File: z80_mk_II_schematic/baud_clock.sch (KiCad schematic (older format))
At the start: 9 parts

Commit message: Lots more work on schematic
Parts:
- gave numbers to parts that had none: 7
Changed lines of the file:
@@
 P 3350 3650
 AR Path="/5F996112/6026683D/602A193D" Ref="U?"  Part="1"
-AR Path="/5F996112/6029665D/602A193D" Ref="U?"  Part="1"
-F 0 "U?" H 3350 3967 50  0000 C CNN
+AR Path="/5F996112/6029665D/602A193D" Ref="U20"  Part="1"
+F 0 "U20" H 3350 3967 50  0000 C CNN
 F 1 "74LS04" H 3350 3876 50  0000 C CNN
 F 2 "" H 3350 3650 50  0001 C CNN
@@
 P 4350 3650
 AR Path="/5F996112/6026683D/602A1943" Ref="U?"  Part="2"
-AR Path="/5F996112/6029665D/602A1943" Ref="U?"  Part="2"
-F 0 "U?" H 4350 3967 50  0000 C CNN
+AR Path="/5F996112/6029665D/602A1943" Ref="U20"  Part="2"
+F 0 "U20" H 4350 3967 50  0000 C CNN
 F 1 "74LS04" H 4350 3876 50  0000 C CNN
 F 2 "" H 4350 3650 50  0001 C CNN
@@
 P 5250 3650
 AR Path="/5F996112/6026683D/602A1949" Ref="U?"  Part="3"
-AR Path="/5F996112/6029665D/602A1949" Ref="U?"  Part="3"
-F 0 "U?" H 5250 3967 50  0000 C CNN
+AR Path="/5F996112/6029665D/602A1949" Ref="U20"  Part="3"
+F 0 "U20" H 5250 3967 50  0000 C CNN
 F 1 "74LS04" H 5250 3876 50  0000 C CNN
 F 2 "" H 5250 3650 50  0001 C CNN
@@
 P 3850 3650
 AR Path="/5F996112/6026683D/602A194F" Ref="C?"  Part="1"
-AR Path="/5F996112/6029665D/602A194F" Ref="C?"  Part="1"
-F 0 "C?" V 3621 3650 50  0000 C CNN
+AR Path="/5F996112/6029665D/602A194F" Ref="C22"  Part="1"
+F 0 "C22" V 3621 3650 50  0000 C CNN
 F 1 "10n" V 3712 3650 50  0000 C CNN
 F 2 "" H 3850 3650 50  0001 C CNN
@@
 P 3300 4050
 AR Path="/5F996112/6026683D/602A1957" Ref="R?"  Part="1"
-AR Path="/5F996112/6029665D/602A1957" Ref="R?"  Part="1"
-F 0 "R?" V 3496 4050 50  0000 C CNN
+AR Path="/5F996112/6029665D/602A1957" Ref="R22"  Part="1"
+F 0 "R22" V 3496 4050 50  0000 C CNN
 F 1 "1K0" V 3405 4050 50  0000 C CNN
 F 2 "" H 3300 4050 50  0001 C CNN
@@
 P 4300 4050
 AR Path="/5F996112/6026683D/602A1964" Ref="R?"  Part="1"
-AR Path="/5F996112/6029665D/602A1964" Ref="R?"  Part="1"
-F 0 "R?" V 4496 4050 50  0000 C CNN
+AR Path="/5F996112/6029665D/602A1964" Ref="R23"  Part="1"
+F 0 "R23" V 4496 4050 50  0000 C CNN
 F 1 "1K0" V 4405 4050 50  0000 C CNN
 F 2 "" H 4300 4050 50  0001 C CNN
@@
 P 4850 3900
 AR Path="/5F996112/6026683D/602A1973" Ref="C?"  Part="1"
-AR Path="/5F996112/6029665D/602A1973" Ref="C?"  Part="1"
-F 0 "C?" H 4942 3946 50  0000 L CNN
+AR Path="/5F996112/6029665D/602A1973" Ref="C23"  Part="1"
+F 0 "C23" H 4942 3946 50  0000 L CNN
 F 1 "47p" H 4942 3855 50  0000 L CNN
 F 2 "" H 4850 3900 50  0001 C CNN
@@
 P 4850 4100
 AR Path="/5F996112/6026683D/602A197C" Ref="#PWR?"  Part="1"
-AR Path="/5F996112/6029665D/602A197C" Ref="#PWR0131"  Part="1"
-F 0 "#PWR0131" H 4850 3850 50  0001 C CNN
+AR Path="/5F996112/6029665D/602A197C" Ref="#PWR093"  Part="1"
+F 0 "#PWR093" H 4850 3850 50  0001 C CNN
 F 1 "GND" H 4855 3927 50  0000 C CNN
 F 2 "" H 4850 4100 50  0001 C CNN
@@
 P 3850 3200
 AR Path="/5F996112/6026683D/602A1983" Ref="Y?"  Part="1"
-AR Path="/5F996112/6029665D/602A1983" Ref="Y?"  Part="1"
-F 0 "Y?" H 3850 3468 50  0000 C CNN
+AR Path="/5F996112/6029665D/602A1983" Ref="Y2"  Part="1"
+F 0 "Y2" H 3850 3468 50  0000 C CNN
 F 1 "2.4576MHz" H 3850 3377 50  0000 C CNN
 F 2 "" H 3850 3200 50  0001 C CNN
@@
 P 6450 3350
 AR Path="/5F996112/6026683D/602A1990" Ref="U?"  Part="1"
-AR Path="/5F996112/6029665D/602A1990" Ref="U?"  Part="1"
-F 0 "U?" H 6450 4331 50  0000 C CNN
-F 1 "74LS197" H 6450 4240 50  0000 C CNN
+AR Path="/5F996112/6029665D/602A1990" Ref="U21"  Part="1"
+F 0 "U21" H 6450 3350 50  0000 C CNN
+F 1 "74LS197" H 6450 3250 50  0000 C CNN
 F 2 "" H 6450 3350 50  0001 C CNN
 F 3 "http://www.ti.com/lit/gpn/sn74LS197" H 6450 3350 50  0001 C CNN
@@
 	5550 3650 5950 3650
 $Comp
-L power:+5V #PWR0132
+L power:+5V #PWR095
 U 1 1 602A26C4
 P 6450 2250
-F 0 "#PWR0132" H 6450 2100 50  0001 C CNN
+F 0 "#PWR095" H 6450 2100 50  0001 C CNN
 F 1 "+5V" H 6465 2423 50  0000 C CNN
 F 2 "" H 6450 2250 50  0001 C CNN
@@
 $EndComp
 $Comp
-L power:+5V #PWR0133
+L power:+5V #PWR094
 U 1 1 602A3344
 P 5750 3250
-F 0 "#PWR0133" H 5750 3100 50  0001 C CNN
+F 0 "#PWR094" H 5750 3100 50  0001 C CNN
 F 1 "+5V" H 5765 3423 50  0000 C CNN
 F 2 "" H 5750 3250 50  0001 C CNN
@@
 P 6450 4150
 AR Path="/5F996112/6026683D/602A41F4" Ref="#PWR?"  Part="1"
-AR Path="/5F996112/6029665D/602A41F4" Ref="#PWR0134"  Part="1"
-F 0 "#PWR0134" H 6450 3900 50  0001 C CNN
+AR Path="/5F996112/6029665D/602A41F4" Ref="#PWR096"  Part="1"
+F 0 "#PWR096" H 6450 3900 50  0001 C CNN
 F 1 "GND" H 6455 3977 50  0000 C CNN
 F 2 "" H 6450 4150 50  0001 C CNN

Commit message: Un-fsck something which made most of the chips into 74LS00 for some very odd reason. Also start to assign footprints.
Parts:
- R22, R23: footprint (none) -> Resistors_ThroughHole:R_Axial_DIN0207_L6.3mm_D2.5mm_P10.16mm_Horizontal
- U20, U21: footprint (none) -> Housings_DIP:DIP-14_W7.62mm
- Y2: footprint (none) -> Crystals:Crystal_HC49-4H_Vertical
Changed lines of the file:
@@
 F 0 "U20" H 3350 3967 50  0000 C CNN
 F 1 "74LS04" H 3350 3876 50  0000 C CNN
-F 2 "" H 3350 3650 50  0001 C CNN
+F 2 "Housings_DIP:DIP-14_W7.62mm" H 3350 3650 50  0001 C CNN
 F 3 "http://www.ti.com/lit/gpn/sn74LS04" H 3350 3650 50  0001 C CNN
 	1    3350 3650
@@
 F 0 "U20" H 4350 3967 50  0000 C CNN
 F 1 "74LS04" H 4350 3876 50  0000 C CNN
-F 2 "" H 4350 3650 50  0001 C CNN
+F 2 "Housings_DIP:DIP-14_W7.62mm" H 4350 3650 50  0001 C CNN
 F 3 "http://www.ti.com/lit/gpn/sn74LS04" H 4350 3650 50  0001 C CNN
 	2    4350 3650
@@
 F 0 "U20" H 5250 3967 50  0000 C CNN
 F 1 "74LS04" H 5250 3876 50  0000 C CNN
-F 2 "" H 5250 3650 50  0001 C CNN
+F 2 "Housings_DIP:DIP-14_W7.62mm" H 5250 3650 50  0001 C CNN
 F 3 "http://www.ti.com/lit/gpn/sn74LS04" H 5250 3650 50  0001 C CNN
 	3    5250 3650
@@
 F 0 "R22" V 3496 4050 50  0000 C CNN
 F 1 "1K0" V 3405 4050 50  0000 C CNN
-F 2 "" H 3300 4050 50  0001 C CNN
+F 2 "Resistors_ThroughHole:R_Axial_DIN0207_L6.3mm_D2.5mm_P10.16mm_Horizontal" H 3300 4050 50  0001 C CNN
 F 3 "~" H 3300 4050 50  0001 C CNN
 	1    3300 4050
@@
 F 0 "R23" V 4496 4050 50  0000 C CNN
 F 1 "1K0" V 4405 4050 50  0000 C CNN
-F 2 "" H 4300 4050 50  0001 C CNN
+F 2 "Resistors_ThroughHole:R_Axial_DIN0207_L6.3mm_D2.5mm_P10.16mm_Horizontal" H 4300 4050 50  0001 C CNN
 F 3 "~" H 4300 4050 50  0001 C CNN
 	1    4300 4050
@@
 F 0 "Y2" H 3850 3468 50  0000 C CNN
 F 1 "2.4576MHz" H 3850 3377 50  0000 C CNN
-F 2 "" H 3850 3200 50  0001 C CNN
+F 2 "Crystals:Crystal_HC49-4H_Vertical" H 3850 3200 50  0001 C CNN
 F 3 "~" H 3850 3200 50  0001 C CNN
 	1    3850 3200
@@
 F 0 "U21" H 6450 3350 50  0000 C CNN
 F 1 "74LS197" H 6450 3250 50  0000 C CNN
-F 2 "" H 6450 3350 50  0001 C CNN
+F 2 "Housings_DIP:DIP-14_W7.62mm" H 6450 3350 50  0001 C CNN
 F 3 "http://www.ti.com/lit/gpn/sn74LS197" H 6450 3350 50  0001 C CNN
 	1    6450 3350

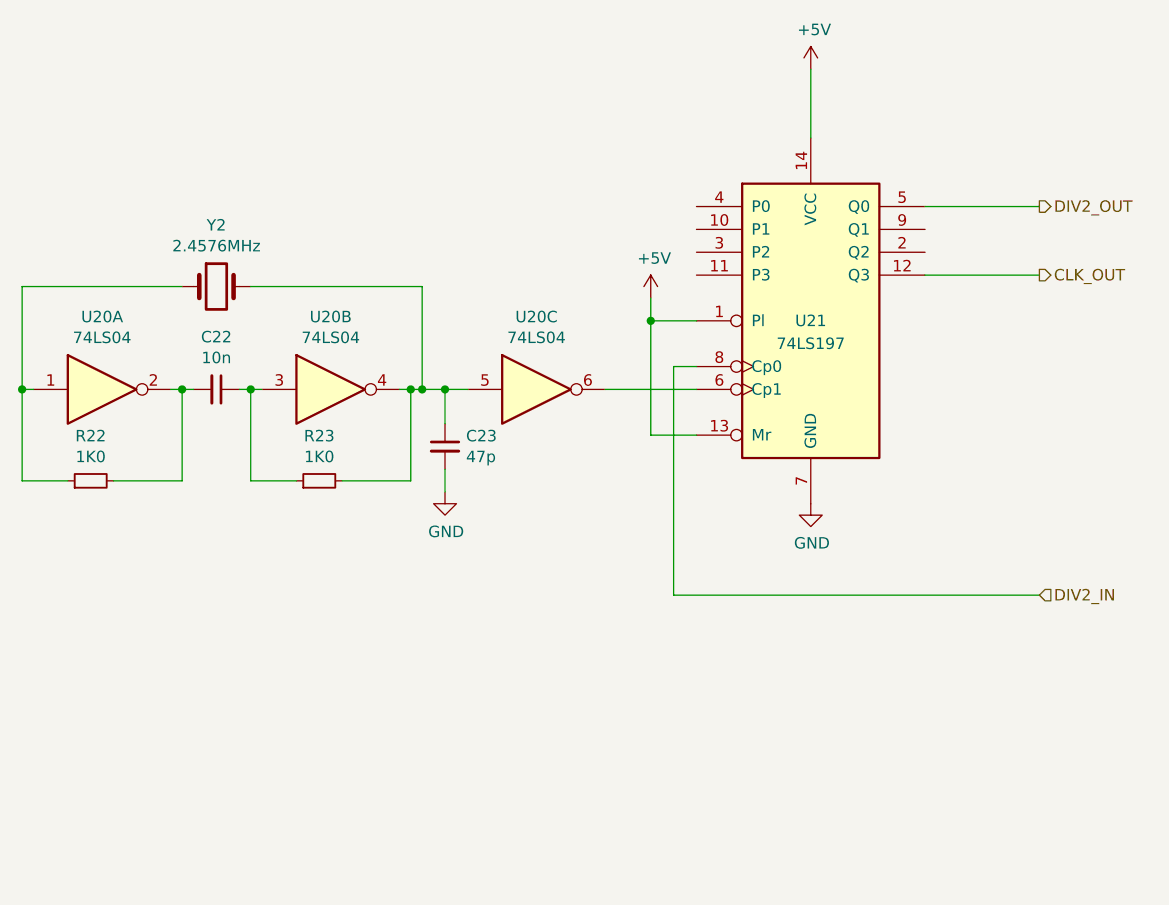
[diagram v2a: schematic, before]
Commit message: Add some no-connection symbols.
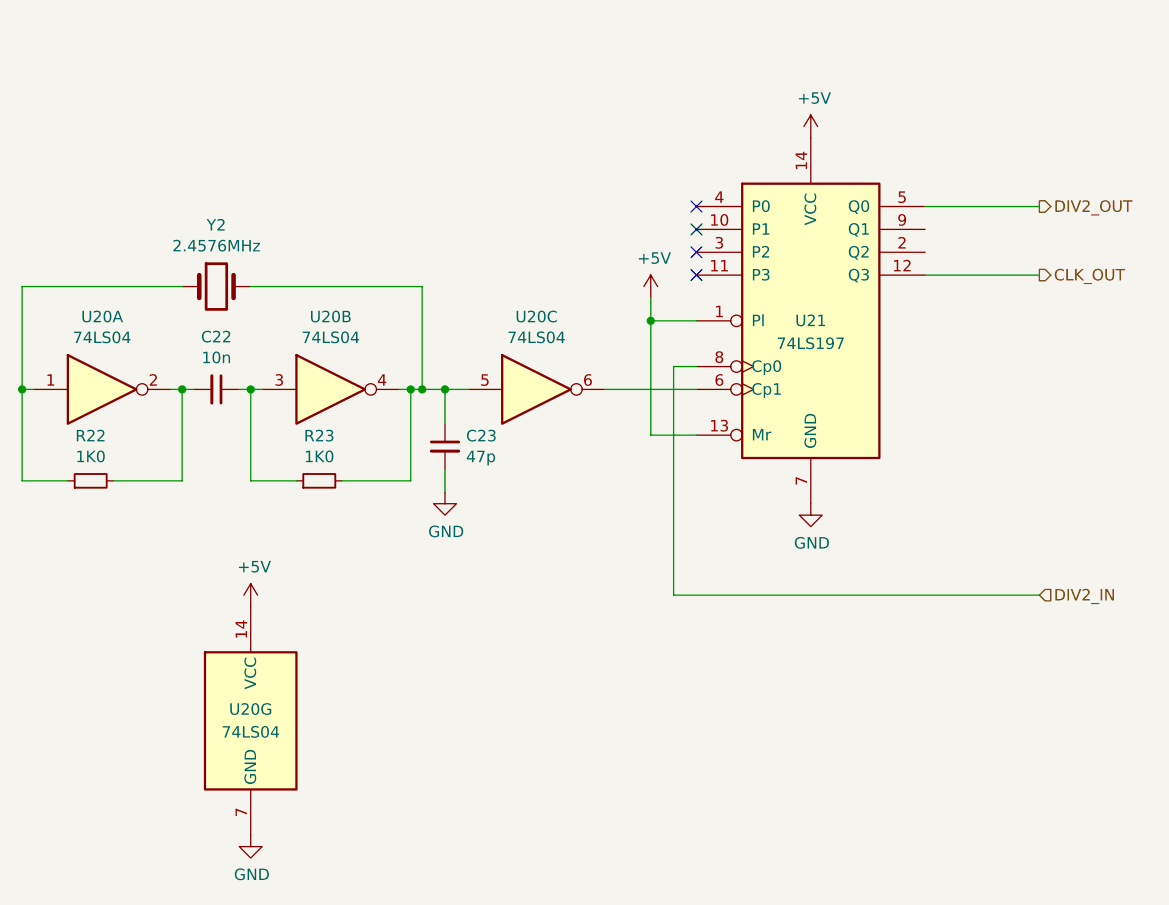
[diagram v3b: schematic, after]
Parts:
- added unit 7 of U20
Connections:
- net +5V: now also U20.14 (VCC)
- net GND: now also U20.7 (GND)
- no-connect marks 0 -> 4
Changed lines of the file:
@@
 L power:+5V #PWR095
 U 1 1 602A26C4
-P 6450 2250
-F 0 "#PWR095" H 6450 2100 50  0001 C CNN
-F 1 "+5V" H 6465 2423 50  0000 C CNN
-F 2 "" H 6450 2250 50  0001 C CNN
-F 3 "" H 6450 2250 50  0001 C CNN
-	1    6450 2250
+P 6450 2550
+F 0 "#PWR095" H 6450 2400 50  0001 C CNN
+F 1 "+5V" H 6465 2723 50  0000 C CNN
+F 2 "" H 6450 2550 50  0001 C CNN
+F 3 "" H 6450 2550 50  0001 C CNN
+	1    6450 2550
 	1    0    0    -1
 $EndComp
@@
 Wire Wire Line
 	5750 3350 5750 3250
-Wire Wire Line
-	6450 2550 6450 2250
 $Comp
 L power:GND #PWR?
@@
 Text HLabel 7450 4550 2    50   Input ~ 0
 DIV2_IN
+$Comp
+L 74xx:74LS04 U?
+U 7 1 5FECADC5
+P 4000 5100
+AR Path="/5F996112/6026683D/5FECADC5" Ref="U?"  Part="3"
+AR Path="/5F996112/6029665D/5FECADC5" Ref="U20"  Part="7"
+F 0 "U20" H 4000 5150 50  0000 C CNN
+F 1 "74LS04" H 4000 5050 50  0000 C CNN
+F 2 "Housings_DIP:DIP-14_W7.62mm" H 4000 5100 50  0001 C CNN
+F 3 "http://www.ti.com/lit/gpn/sn74LS04" H 4000 5100 50  0001 C CNN
+	7    4000 5100
+	1    0    0    -1
+$EndComp
+$Comp
+L power:GND #PWR?
+U 1 1 5FECCA0F
+P 4000 5600
+AR Path="/5F996112/6026683D/5FECCA0F" Ref="#PWR?"  Part="1"
+AR Path="/5F996112/6029665D/5FECCA0F" Ref="#PWR?"  Part="1"
+F 0 "#PWR?" H 4000 5350 50  0001 C CNN
+F 1 "GND" H 4005 5427 50  0000 C CNN
+F 2 "" H 4000 5600 50  0001 C CNN
+F 3 "" H 4000 5600 50  0001 C CNN
+	1    4000 5600
+	1    0    0    -1
+$EndComp
+$Comp
+L power:+5V #PWR?
+U 1 1 5FECD6AA
+P 4000 4600
+F 0 "#PWR?" H 4000 4450 50  0001 C CNN
+F 1 "+5V" H 4015 4773 50  0000 C CNN
+F 2 "" H 4000 4600 50  0001 C CNN
+F 3 "" H 4000 4600 50  0001 C CNN
+	1    4000 4600
+	1    0    0    -1
+$EndComp
+NoConn ~ 5950 2850
+NoConn ~ 5950 2950
+NoConn ~ 5950 3050
+NoConn ~ 5950 3150
 $EndSCHEMATC

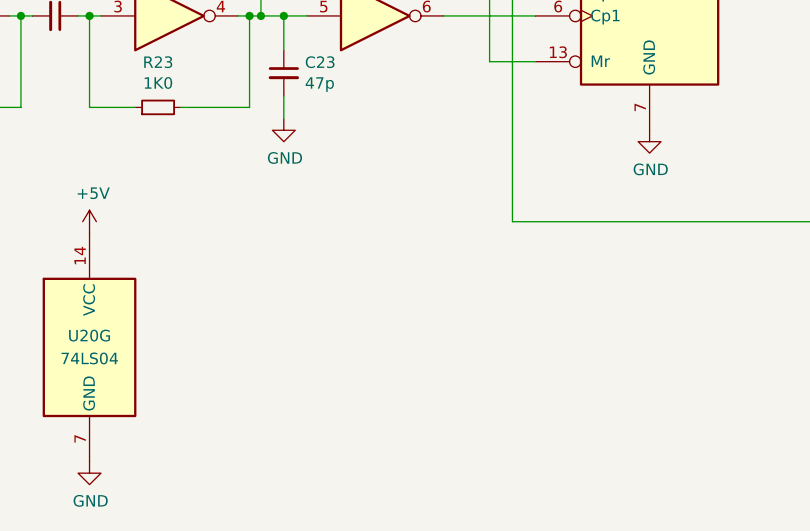
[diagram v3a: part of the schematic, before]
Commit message: Add some missing gates and wiring.
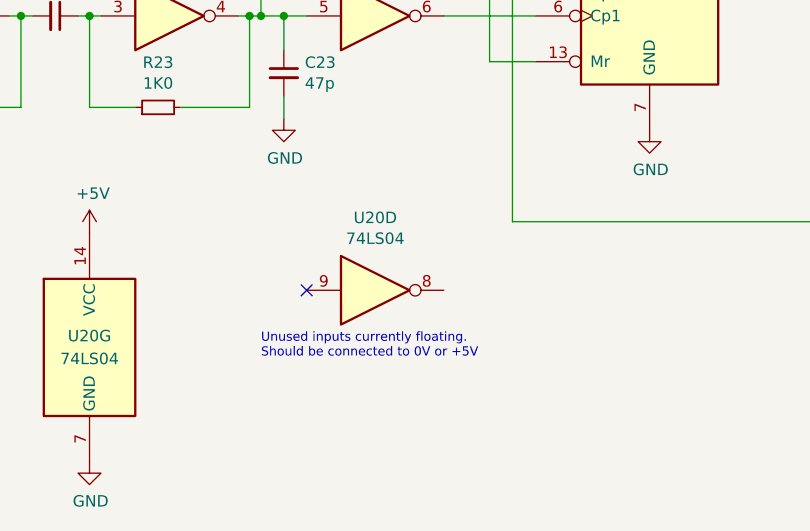
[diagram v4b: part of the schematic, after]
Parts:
- added unit 4 of U20
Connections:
- no-connect marks 4 -> 5
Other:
- note added: "Unused inputs currently floating.\nShould be connected to 0V or +5V"
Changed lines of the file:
@@
 P 4000 5600
 AR Path="/5F996112/6026683D/5FECCA0F" Ref="#PWR?"  Part="1"
-AR Path="/5F996112/6029665D/5FECCA0F" Ref="#PWR?"  Part="1"
-F 0 "#PWR?" H 4000 5350 50  0001 C CNN
+AR Path="/5F996112/6029665D/5FECCA0F" Ref="#PWR0116"  Part="1"
+F 0 "#PWR0116" H 4000 5350 50  0001 C CNN
 F 1 "GND" H 4005 5427 50  0000 C CNN
 F 2 "" H 4000 5600 50  0001 C CNN
@@
 $EndComp
 $Comp
-L power:+5V #PWR?
+L power:+5V #PWR0117
 U 1 1 5FECD6AA
 P 4000 4600
-F 0 "#PWR?" H 4000 4450 50  0001 C CNN
+F 0 "#PWR0117" H 4000 4450 50  0001 C CNN
 F 1 "+5V" H 4015 4773 50  0000 C CNN
 F 2 "" H 4000 4600 50  0001 C CNN
@@
 NoConn ~ 5950 3050
 NoConn ~ 5950 3150
+$Comp
+L 74xx:74LS04 U?
+U 4 1 5FB2EC4A
+P 5250 4850
+AR Path="/5F996112/6026683D/5FB2EC4A" Ref="U?"  Part="3"
+AR Path="/5F996112/6029665D/5FB2EC4A" Ref="U20"  Part="4"
+F 0 "U20" H 5250 5167 50  0000 C CNN
+F 1 "74LS04" H 5250 5076 50  0000 C CNN
+F 2 "Housings_DIP:DIP-14_W7.62mm" H 5250 4850 50  0001 C CNN
+F 3 "http://www.ti.com/lit/gpn/sn74LS04" H 5250 4850 50  0001 C CNN
+	4    5250 4850
+	1    0    0    -1
+$EndComp
+NoConn ~ 4950 4850
+Text Notes 4750 5150 0    40   ~ 0
+Unused inputs currently floating.\nShould be connected to 0V or +5V
 $EndSCHEMATC
